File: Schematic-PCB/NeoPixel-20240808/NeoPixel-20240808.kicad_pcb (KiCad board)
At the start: 2 copper layers, 112 x 112 mm, 33 parts, among them J1 Conn_01x05_Pin

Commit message: add: NeoPixel基板の3Dモデルを出力した
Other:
- board text added: "NeoPixel-Board #002"

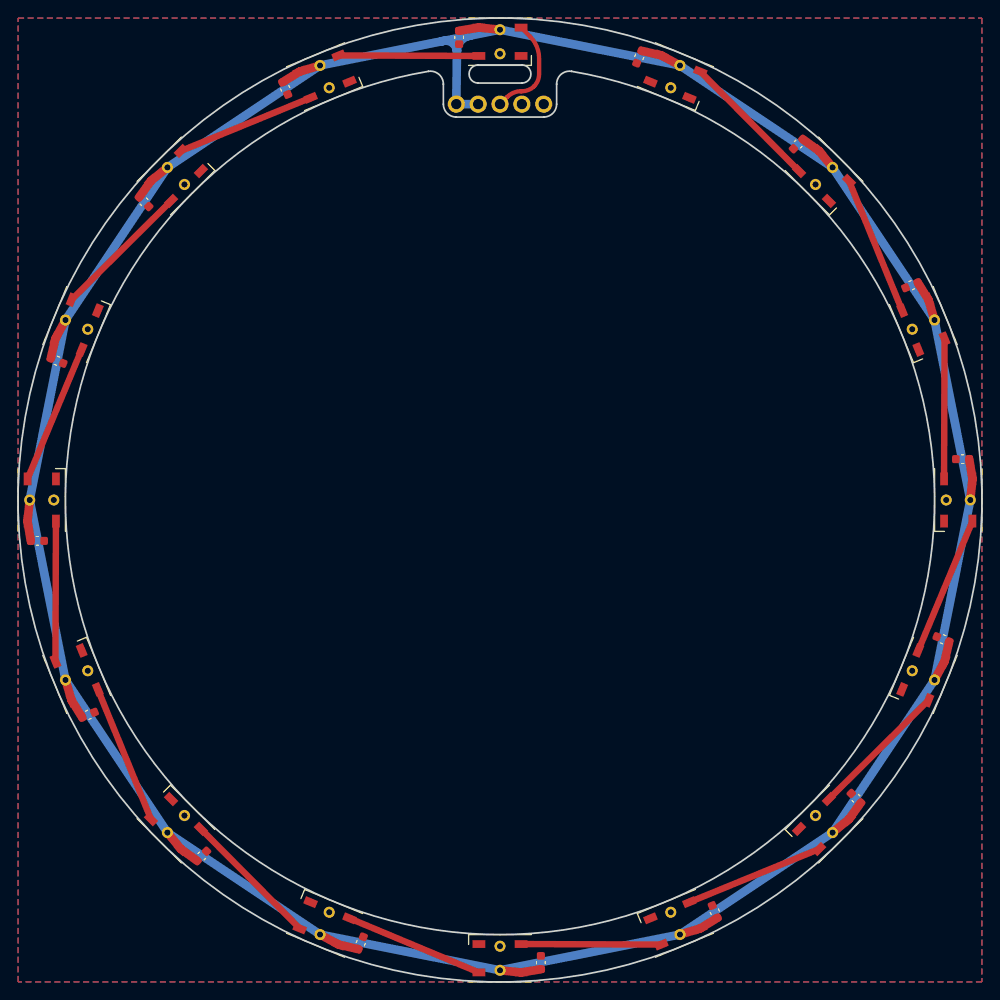
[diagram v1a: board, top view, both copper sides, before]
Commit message: update: メイン基板とNeoPixel基板の発注用ファイルを出力したりした
NeoPixel基板はコネクタを1コ→3コに増やした
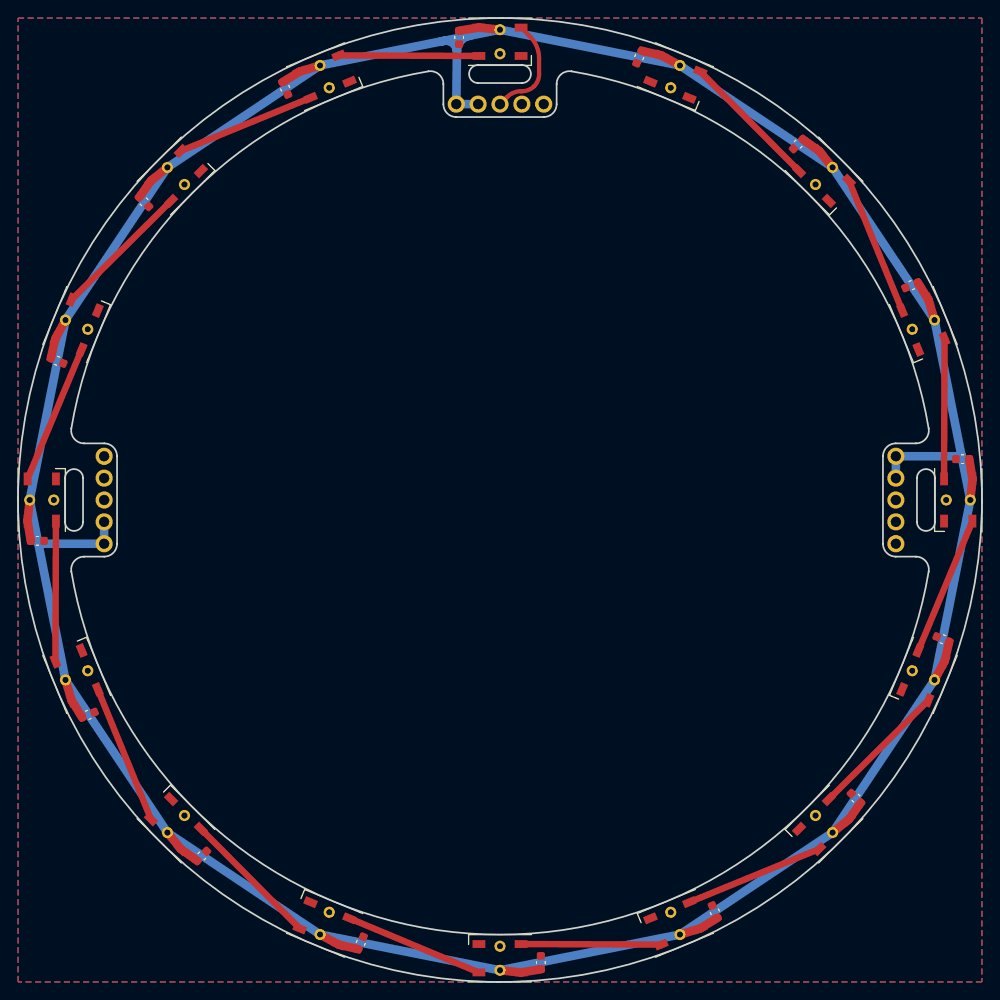
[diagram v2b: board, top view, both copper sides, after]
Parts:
- added J2: Conn_01x05_Pin, @2024TOINIOT2-NeoPixel:Connector, F.Cu at (46.0, 0.00)
- added J3: Conn_01x05_Pin, @2024TOINIOT2-NeoPixel:Connector, F.Cu at (-46.0, 0.00)
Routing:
- net +5V: track 431.4 -> 451.8 mm
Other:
- outline, holes or cut-outs redrawn
